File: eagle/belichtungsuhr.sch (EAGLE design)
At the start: 1 part

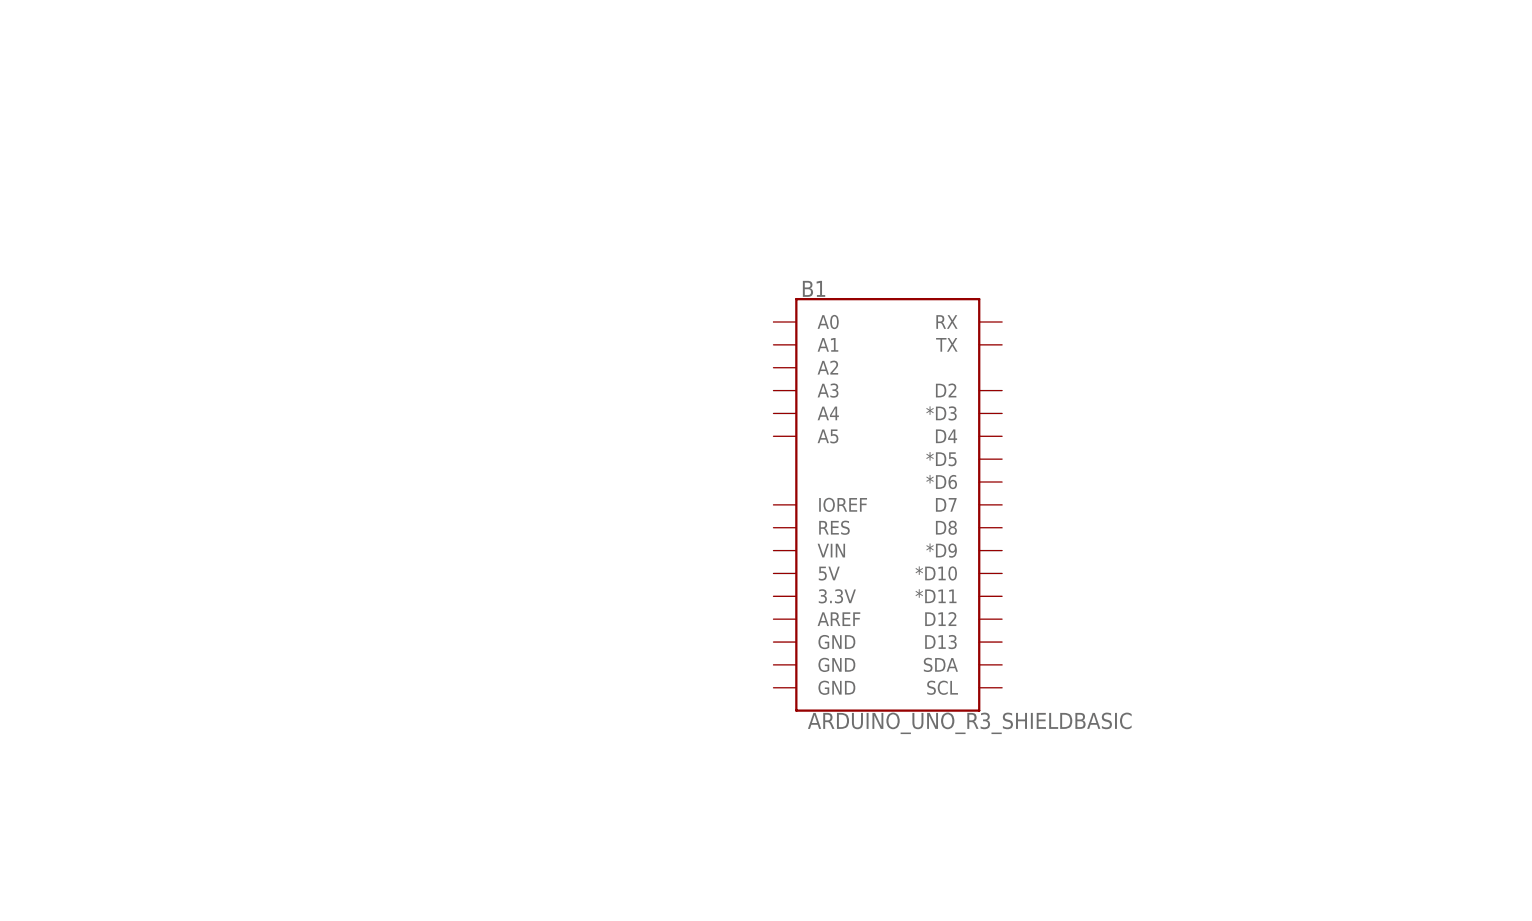
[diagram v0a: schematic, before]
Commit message: Added LCD
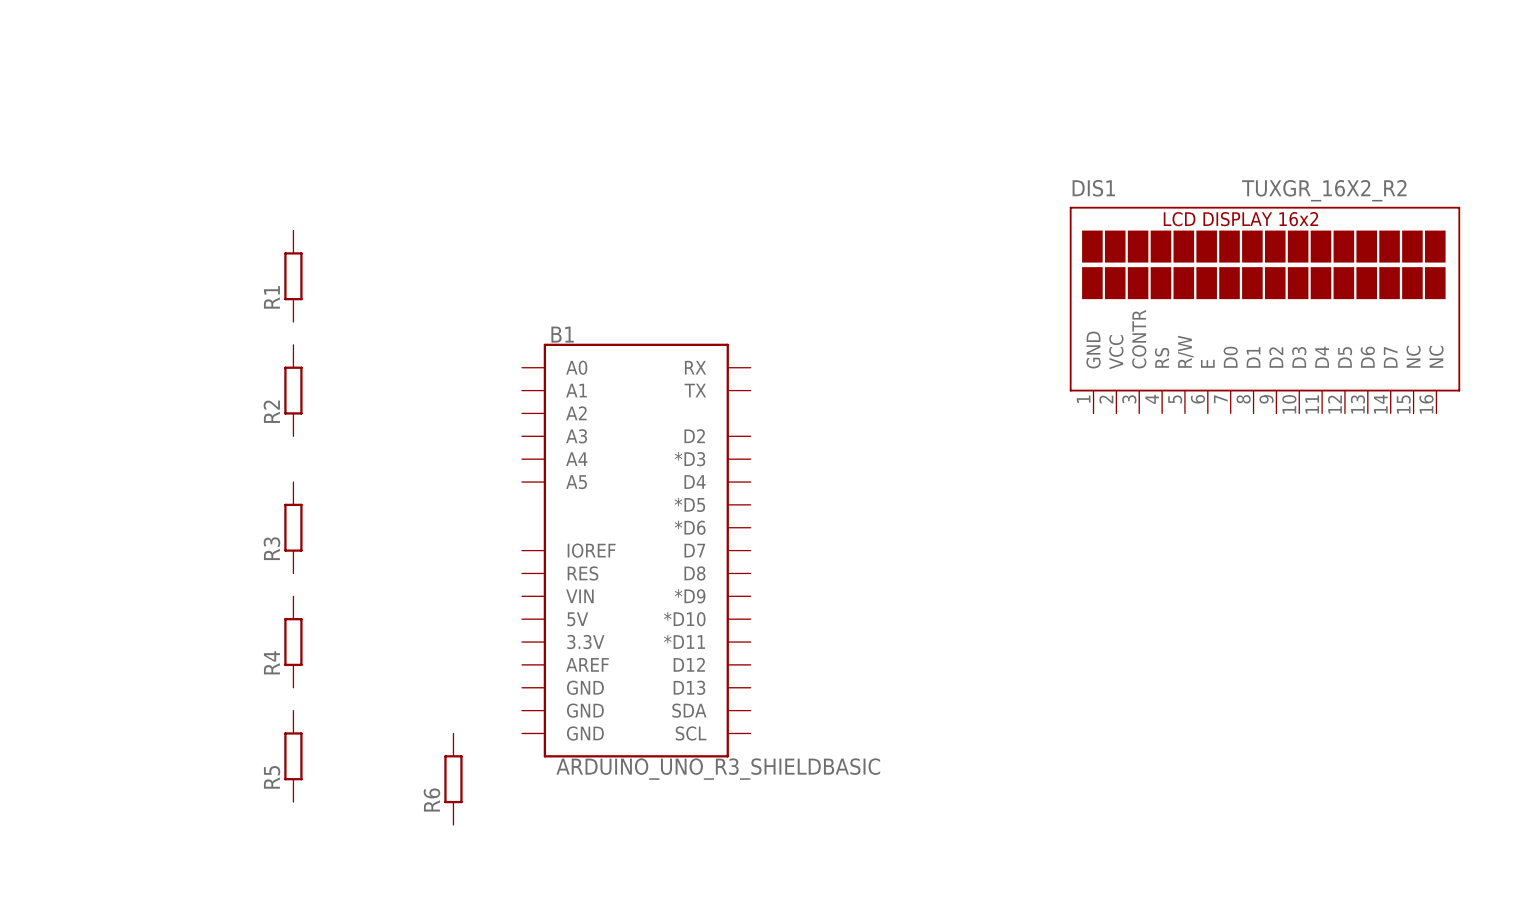
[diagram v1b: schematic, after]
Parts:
- added DIS1: TUXGR_16X2_R2, display-lcd:TUXGR_16X2_R2
- added R1, R2, R3, R4, R5, R6: (no value), rcl:R-EU_0204/7
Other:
- moved on the sheet: B1
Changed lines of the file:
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@@
 <parts>
 <part name="B1" library="SparkFun-Boards" library_urn="urn:adsk.eagle:library:509" deviceset="ARDUINO_UNO_R3_SHIELD" device="BASIC" package3d_urn="urn:adsk.eagle:package:37321/1"/>
+<part name="DIS1" library="display-lcd" library_urn="urn:adsk.eagle:library:214" deviceset="TUXGR_16X2_R2" device="" package3d_urn="urn:adsk.eagle:package:13139/1"/>
+<part name="R1" library="rcl" library_urn="urn:adsk.eagle:library:334" deviceset="R-EU_" device="0204/7" package3d_urn="urn:adsk.eagle:package:23498/2"/>
+<part name="R2" library="rcl" library_urn="urn:adsk.eagle:library:334" deviceset="R-EU_" device="0204/7" package3d_urn="urn:adsk.eagle:package:23498/2"/>
+<part name="R3" library="rcl" library_urn="urn:adsk.eagle:library:334" deviceset="R-EU_" device="0204/7" package3d_urn="urn:adsk.eagle:package:23498/2"/>
+<part name="R4" library="rcl" library_urn="urn:adsk.eagle:library:334" deviceset="R-EU_" device="0204/7" package3d_urn="urn:adsk.eagle:package:23498/2"/>
+<part name="R5" library="rcl" library_urn="urn:adsk.eagle:library:334" deviceset="R-EU_" device="0204/7" package3d_urn="urn:adsk.eagle:package:23498/2"/>
+<part name="R6" library="rcl" library_urn="urn:adsk.eagle:library:334" deviceset="R-EU_" device="0204/7" package3d_urn="urn:adsk.eagle:package:23498/2"/>
 </parts>
 <sheets>
@@
 </plain>
 <instances>
-<instance part="B1" gate="G$1" x="40.64" y="50.8" smashed="yes">
-<attribute name="NAME" x="30.988" y="71.374" size="1.778" layer="95" font="vector"/>
-<attribute name="VALUE" x="31.75" y="25.146" size="1.778" layer="96" font="vector" align="top-left"/>
+<instance part="B1" gate="G$1" x="12.7" y="45.72" smashed="yes">
+<attribute name="NAME" x="3.048" y="66.294" size="1.778" layer="95" font="vector"/>
+<attribute name="VALUE" x="3.81" y="20.066" size="1.778" layer="96" font="vector" align="top-left"/>
+</instance>
+<instance part="DIS1" gate="G$1" x="81.28" y="68.58" smashed="yes">
+<attribute name="NAME" x="60.96" y="82.55" size="1.778" layer="95"/>
+<attribute name="VALUE" x="80.01" y="82.55" size="1.778" layer="96"/>
+</instance>
+<instance part="R1" gate="G$1" x="-25.4" y="73.66" smashed="yes" rot="R90">
+<attribute name="NAME" x="-26.8986" y="69.85" size="1.778" layer="95" rot="R90"/>
+<attribute name="VALUE" x="-22.098" y="69.85" size="1.778" layer="96" rot="R90"/>
+</instance>
+<instance part="R2" gate="G$1" x="-25.4" y="60.96" smashed="yes" rot="R90">
+<attribute name="NAME" x="-26.8986" y="57.15" size="1.778" layer="95" rot="R90"/>
+<attribute name="VALUE" x="-22.098" y="57.15" size="1.778" layer="96" rot="R90"/>
+</instance>
+<instance part="R3" gate="G$1" x="-25.4" y="45.72" smashed="yes" rot="R90">
+<attribute name="NAME" x="-26.8986" y="41.91" size="1.778" layer="95" rot="R90"/>
+<attribute name="VALUE" x="-22.098" y="41.91" size="1.778" layer="96" rot="R90"/>
+</instance>
+<instance part="R4" gate="G$1" x="-25.4" y="33.02" smashed="yes" rot="R90">
+<attribute name="NAME" x="-26.8986" y="29.21" size="1.778" layer="95" rot="R90"/>
+<attribute name="VALUE" x="-22.098" y="29.21" size="1.778" layer="96" rot="R90"/>
+</instance>
+<instance part="R5" gate="G$1" x="-25.4" y="20.32" smashed="yes" rot="R90">
+<attribute name="NAME" x="-26.8986" y="16.51" size="1.778" layer="95" rot="R90"/>
+<attribute name="VALUE" x="-22.098" y="16.51" size="1.778" layer="96" rot="R90"/>
+</instance>
+<instance part="R6" gate="G$1" x="-7.62" y="17.78" smashed="yes" rot="R90">
+<attribute name="NAME" x="-9.1186" y="13.97" size="1.778" layer="95" rot="R90"/>
+<attribute name="VALUE" x="-4.318" y="13.97" size="1.778" layer="96" rot="R90"/>
 </instance>
 </instances>
@@
 packages will not be understood (or retained) with this version.
 </note>
+<note version="8.4" severity="warning">
+Since Version 8.4, EAGLE supports properties for SPICE simulation.
+Probes in schematics and SPICE mapping objects found in parts and library devices
+will not be understood with this version. Update EAGLE to the latest version
+for full support of SPICE simulation.
+</note>
 </compatibility>

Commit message: Eagle PCB changes
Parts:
- added JP2: (no value), pinhead:PINHD-1X7
- added JP3: (no value), pinhead:PINHD-2X2
- added JP4: (no value), pinhead:PINHD-2X5
- added R10: (no value), pot:TRIM_EU-LI10
- added R9: (no value), rcl:R-EU_0204/7
- added RESET, S1, S2, S3, S4, S5: (no value), switch-omron:10-XX
- R1, R2, R3, R4, R5: value (none) -> 1K
- R6: value (none) -> 100K
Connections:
- new net +5V: B1.5V, DIS1.VCC, R1.2, R10.E, S1.P
- new net GND: B1.GND@0, DIS1.GND, DIS1.NC@2, DIS1.R/W, R10.A, R5.1, R6.1, RESET.P
- new net N$1: R1.1, R2.2, S2.P
- new net N$10: B1.SDA, JP3.4
- new net N$11: DIS1.CONTR, R10.S
- new net N$2: R2.1, R3.2, S3.P
- new net N$3: R3.1, R4.2, S4.P
- new net N$4: R4.1, R5.2, S5.P
- new net N$5: B1.RES, RESET.S
- new net N$6: B1.A5, R6.2, S1.S, S2.S, S3.S, S4.S, S5.S
- new net N$7: B1.AREF, JP3.1
- new net N$8: B1.IOREF, JP3.3
- new net N$9: B1.SCL, JP3.2
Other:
- moved on the sheet: B1, DIS1, R1, R2, R3, R4, R5, R6
